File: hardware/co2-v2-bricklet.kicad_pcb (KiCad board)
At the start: 2 copper layers, 35 x 40 mm, 27 parts, among them P1 CON-SENSOR2, P2 DEBUG, P3 BOOT, U1 XMC1XXX24, U2 DRILL, U3 DRILL, U4 DRILL, U5 DRILL, U6 SCD30

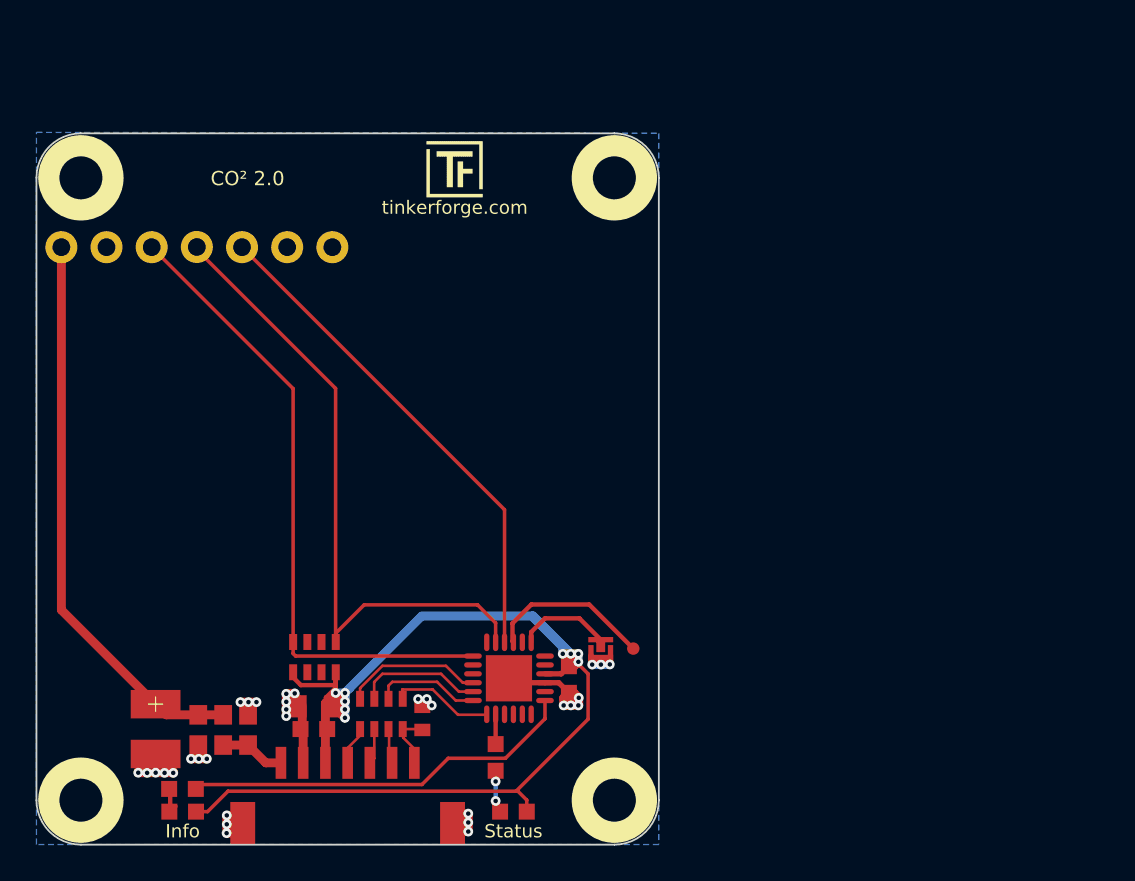
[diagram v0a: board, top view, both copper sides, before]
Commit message: fix grid origin, change name
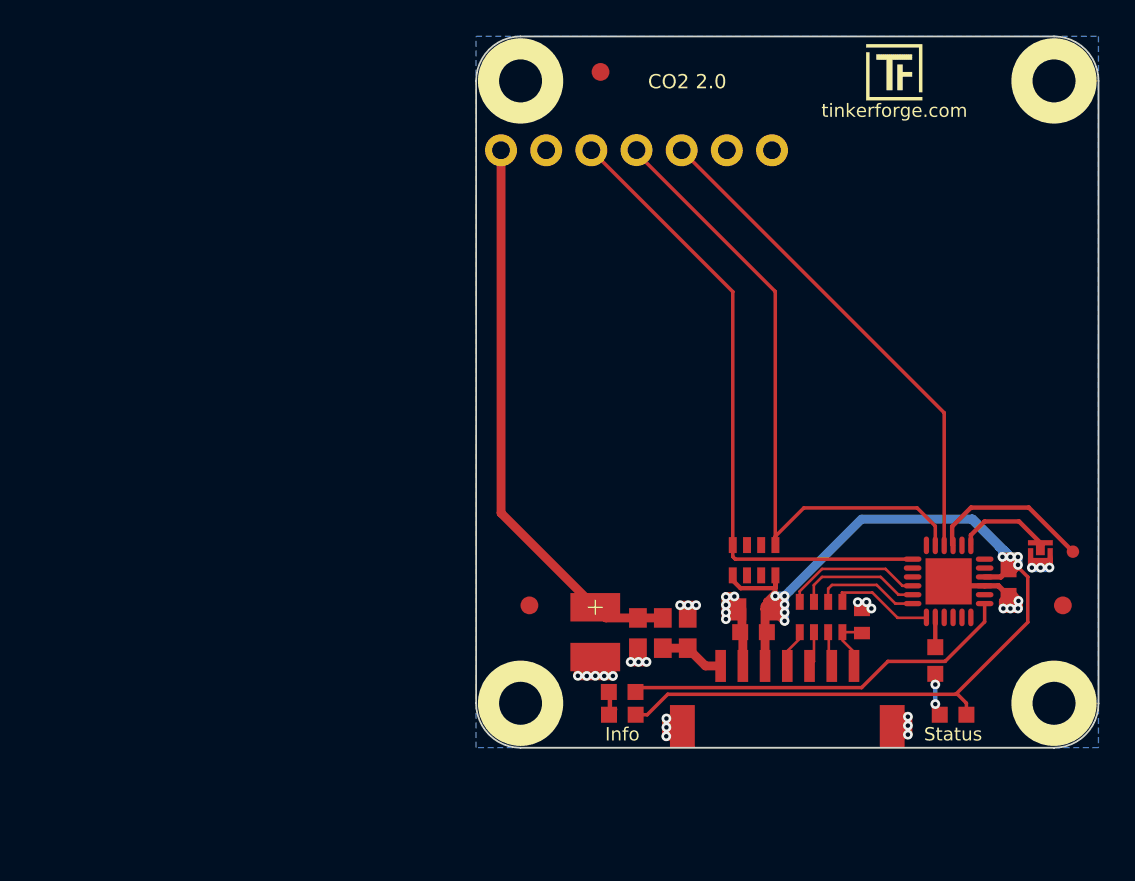
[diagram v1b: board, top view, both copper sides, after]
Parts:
- added Fiducial_Mark: VAL**, kicad-libraries:Fiducial_Mark, F.Cu at (154.0, 106.0)
- added Fiducial_Mark: VAL**, kicad-libraries:Fiducial_Mark, F.Cu at (124.0, 106.0)
- added Fiducial_Mark: VAL**, kicad-libraries:Fiducial_Mark, F.Cu at (128.0, 76.0)
- moved P3 25.3 mm to (152.7, 103.0)
- moved C3 25.3 mm to (136.6, 107.5)
- moved C5 25.3 mm to (132.9, 107.6)
- moved C6 25.3 mm to (130.1, 107.6)
- moved G*** 25.3 mm to (142.9, 74.4)
- moved L1 25.3 mm to (131.5, 107.6)
- moved P1 25.3 mm to (138.5, 114.0)
- moved R2 25.3 mm to (129.2, 110.9)
- moved C1 25.3 mm to (142.7, 106.9)
- moved C2 25.3 mm to (136.7, 106.2)
- moved C4 25.3 mm to (150.9, 104.7)
- moved G*** 25.3 mm to (138.5, 92.2)
- moved P2 25.3 mm to (154.6, 103.0)
- moved R1 25.3 mm to (146.8, 109.1)
- moved RP1 25.3 mm to (140.4, 106.7)
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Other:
- board text added: "CO2 2.0"
- board text removed: "CO² 2.0"

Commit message: changed processor to XMC1302
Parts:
- U1: value XMC1XXX24 -> XMC1302
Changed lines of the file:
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@@
       (effects (font (size 0.3 0.3) (thickness 0.075)))
     )
-    (fp_text value XMC1XXX24 (at 0 0.8 90) (layer F.Fab)
+    (fp_text value XMC1302 (at 0 0.8 90) (layer F.Fab)
       (effects (font (size 0.3 0.3) (thickness 0.075)))
     )
